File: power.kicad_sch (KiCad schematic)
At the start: 0 parts

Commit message: More work. Getting there.
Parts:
- added C18, C19, C20, C21, C22, C23, C24, C25, C26, C27, C28, C29, C30, C31: 0.1uF, symbol Device:C_Small
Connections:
- new net: C30.2, C31.2
- new net GND: C18.2, C19.2, C20.2, C21.2, C22.2, C23.2, C24.2, C25.2, C26.2, C27.2, C28.2, C29.2
- new net V5: C18.1, C19.1, C20.1, C21.1, C22.1, C23.1, C24.1, C25.1, C26.1, C27.1, C28.1, C29.1, C30.1, C31.1
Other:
- note added: "Bottom Side"
- note added: "Top Side"

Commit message: Latest updates
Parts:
- added C33: 47uF, symbol Device:C_Polarized_Small
- added D1: MBRS140, Diode_SMD:D_SOD-123F, symbol Device:D_Small
- added F1: ASMDC185F/33-2, symbol Device:Polyfuse_Small
- C18, C19, C20, C21, C22, C23, C24, C25, C26, C27, C28, C29, C30, C31: footprint (none) -> Capacitor_SMD:C_0603_1608Metric_Pad1.08x0.95mm_HandSolder
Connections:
- net GND: now also C33.2
- net V5: now also C33.1, D1.2 (A)
- new net: D1.1 (K), F1.1
- new net SCSI_TERMPWR: F1.2

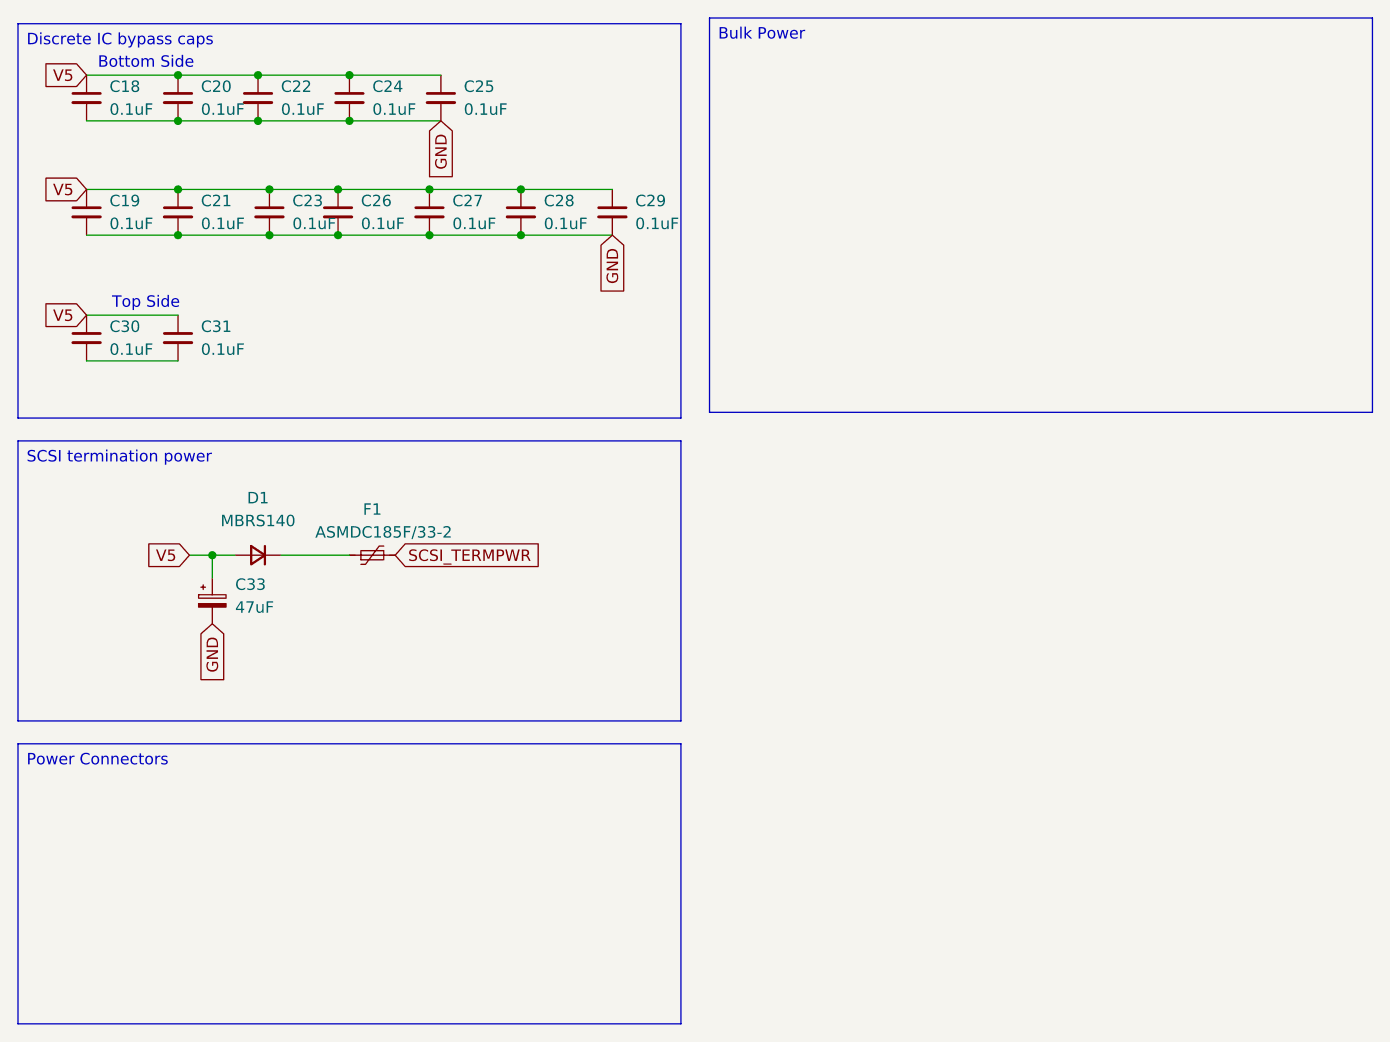
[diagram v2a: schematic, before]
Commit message: Finished first pass at new schematics
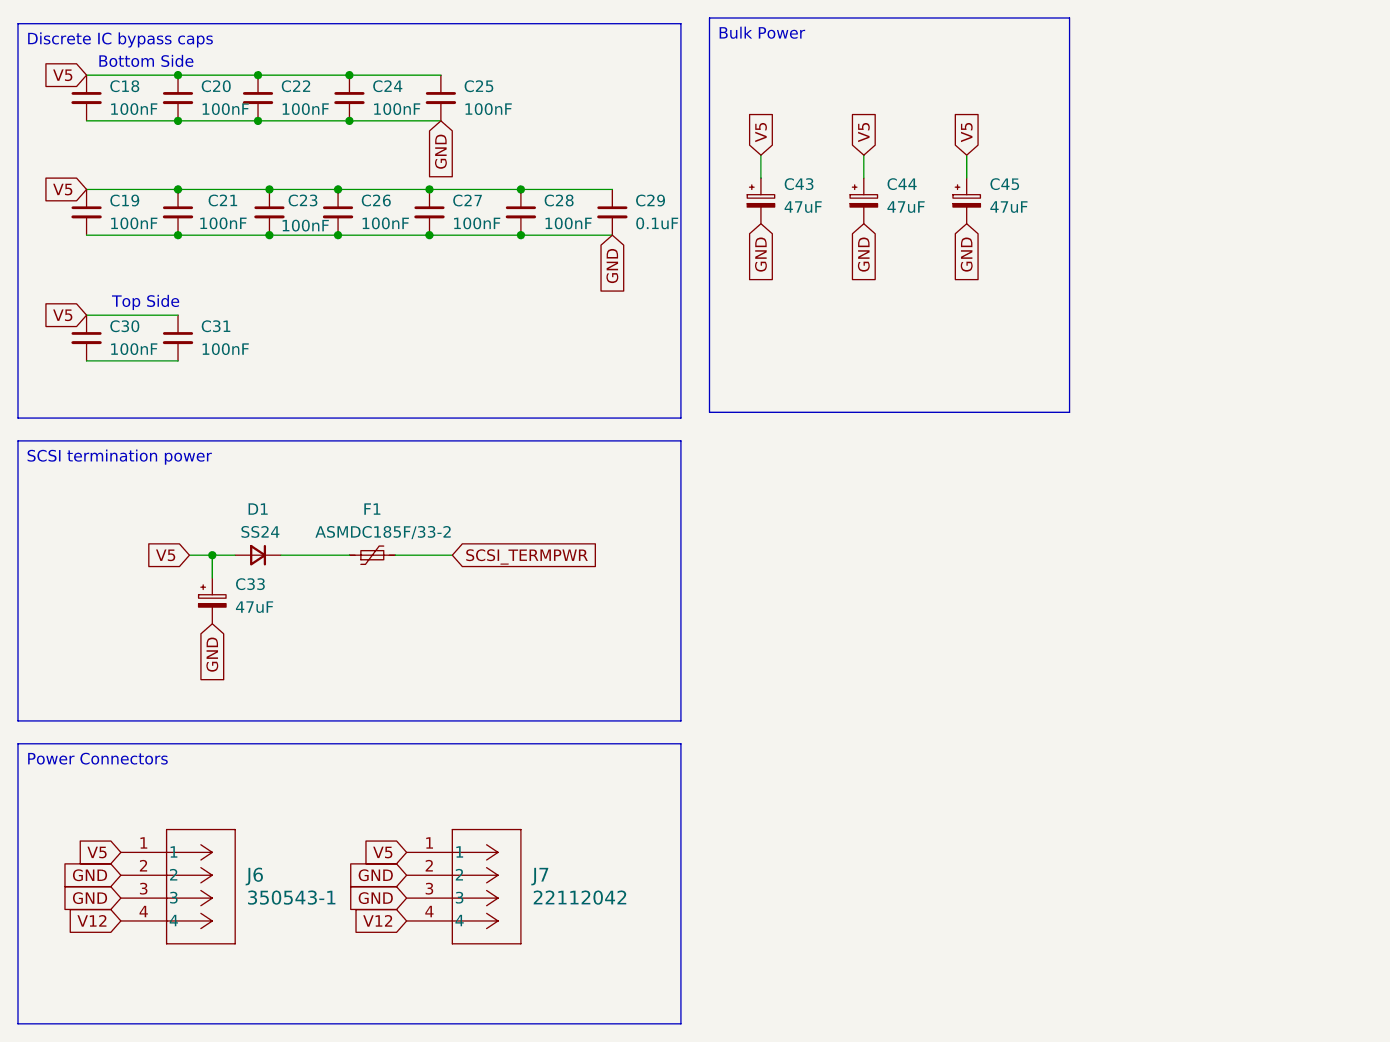
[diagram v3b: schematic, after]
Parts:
- added C43, C44, C45: 47uF, Capacitor_SMD:CP_Elec_6.3x7.7, symbol Device:C_Polarized_Small
- added J6: 350543-1, 350543_1:CONN_350543-1_TYC, symbol 350543_1:350543-1
- added J7: 22112042, 22112042:CONN_A-6373-04A_MOL, symbol 22112042:22112042
- C18, C19, C20, C21, C22, C23, C24, C25, C26, C27, C28, C30, C31: value 0.1uF -> 100nF
- C33: footprint (none) -> Capacitor_SMD:CP_Elec_6.3x7.7
- D1: value MBRS140 -> SS24; footprint Diode_SMD:D_SOD-123F -> Diode_SMD:D_SMA_Handsoldering
- F1: footprint (none) -> Fuse:Fuse_2920_7451Metric_Pad2.10x5.45mm_HandSolder
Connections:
- net GND: now also C43.2, C44.2, C45.2, J6.2, J6.3, J7.2, J7.3
- net V5: now also C43.1, C44.1, C45.1, J6.1, J7.1
- new net V12: J6.4, J7.4

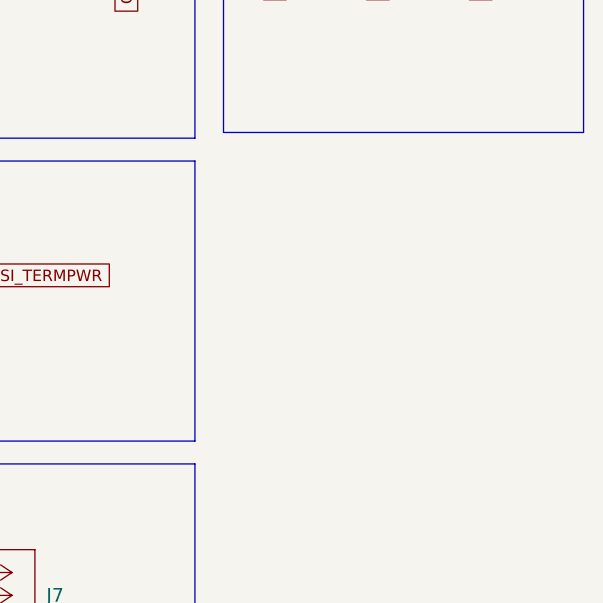
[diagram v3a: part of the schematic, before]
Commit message: Connect VCCINT on CPLD, add GND and V5 to power symbols
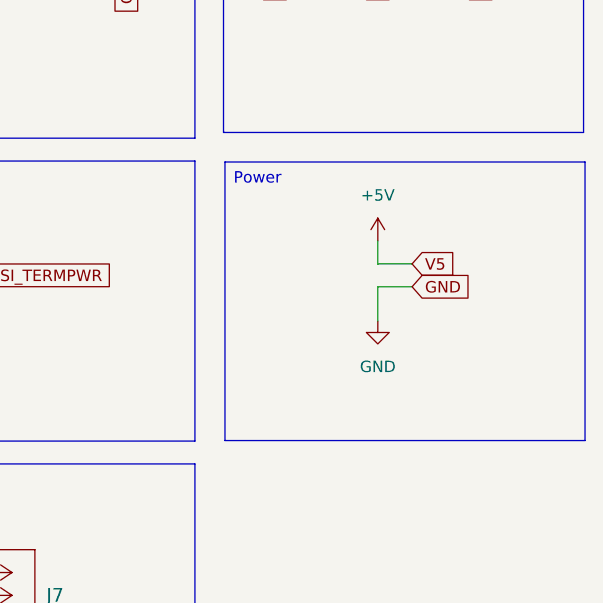
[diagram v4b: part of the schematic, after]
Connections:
- net V5 renamed +5V
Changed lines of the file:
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@@
+		)
+	)
+	(text_box "Power\n"
+		(exclude_from_sim no)
+		(at 98.5884 67.4165 0)
+		(size 40.005 30.9505)
+		(margins 0.9525 0.9525 0.9525 0.9525)
+		(stroke
+			(width 0)
+			(type solid)
+		)
+		(fill
+			(type none)
+		)
+		(effects
+			(font
+				(size 1.27 1.27)
+			)
+			(justify left top)
 		)
 	)
@@
 	(wire
 		(pts
+			(xy 115.57 81.28) (xy 119.38 81.28)
+		)
+		(stroke
+			(width 0)
+			(type default)
+		)
+	)
+	(wire
+		(pts
 			(xy 39.37 44.45) (xy 49.53 44.45)
 		)
@@
 	(wire
 		(pts
+			(xy 115.57 76.2) (xy 115.57 78.74)
+		)
+		(stroke
+			(width 0)
+			(type default)
+		)
+	)
+	(wire
+		(pts
 			(xy 67.31 44.45) (xy 77.47 44.45)
 		)
@@
 	(wire
 		(pts
+			(xy 115.57 85.09) (xy 115.57 81.28)
+		)
+		(stroke
+			(width 0)
+			(type default)
+		)
+	)
+	(wire
+		(pts
 			(xy 69.85 80.01) (xy 63.5 80.01)
 		)
@@
 	(wire
 		(pts
+			(xy 115.57 78.74) (xy 119.38 78.74)
+		)
+		(stroke
+			(width 0)
+			(type default)
+		)
+	)
+	(wire
+		(pts
 			(xy 58.42 26.67) (xy 68.58 26.67)
 		)
@@
 		)
 	)
+	(global_label "GND"
+		(shape input)
+		(at 119.38 81.28 0)
+		(fields_autoplaced yes)
+		(effects
+			(font
+				(size 1.27 1.27)
+			)
+			(justify left)
+		)
+		(property "Intersheetrefs" "${INTERSHEET_REFS}"
+			(at 126.2357 81.28 0)
+			(effects
+				(font
+					(size 1.27 1.27)
+				)
+				(justify left)
+				(hide yes)
+			)
+		)
+	)
 	(global_label "V5"
 		(shape input)
@@
 				)
 				(justify right)
+				(hide yes)
+			)
+		)
+	)
+	(global_label "V5"
+		(shape input)
+		(at 119.38 78.74 0)
+		(fields_autoplaced yes)
+		(effects
+			(font
+				(size 1.27 1.27)
+			)
+			(justify left)
+		)
+		(property "Intersheetrefs" "${INTERSHEET_REFS}"
+			(at 124.6633 78.74 0)
+			(effects
+				(font
+					(size 1.27 1.27)
+				)
+				(justify left)
 				(hide yes)
 			)
@@
 	)
 	(symbol
+		(lib_id "power:GND")
+		(at 115.57 85.09 0)
+		(unit 1)
+		(exclude_from_sim no)
+		(in_bom yes)
+		(on_board yes)
+		(dnp no)
+		(fields_autoplaced yes)
+		(property "Reference" "#PWR03"
+			(at 115.57 91.44 0)
+			(effects
+				(font
+					(size 1.27 1.27)
+				)
+				(hide yes)
+			)
+		)
+		(property "Value" "GND"
+			(at 115.57 90.17 0)
+			(effects
+				(font
+					(size 1.27 1.27)
+				)
+			)
+		)
+		(property "Footprint" ""
+			(at 115.57 85.09 0)
+			(effects
+				(font
+					(size 1.27 1.27)
+				)
+				(hide yes)
+			)
+		)
+		(property "Datasheet" ""
+			(at 115.57 85.09 0)
+			(effects
+				(font
+					(size 1.27 1.27)
+				)
+				(hide yes)
+			)
+		)
+		(property "Description" "Power symbol creates a global label with name \"GND\" , ground"
+			(at 115.57 85.09 0)
+			(effects
+				(font
+					(size 1.27 1.27)
+				)
+				(hide yes)
+			)
+		)
+		(pin "1"
+		)
+		(instances
+			(project ""
+				(path "/8f9f4021-47aa-41d9-bea7-f6ccf72098bb/166c366c-e5f9-4398-87d9-75fc4b57be99"
+					(reference "#PWR03")
+					(unit 1)
+				)
+			)
+		)
+	)
+	(symbol
 		(lib_id "Device:C_Small")
 		(at 87.63 41.91 0)
@@
 					(unit 1)
 				)
+			)
+		)
+	)
+	(symbol
+		(lib_id "power:+5V")
+		(at 115.57 76.2 0)
+		(unit 1)
+		(exclude_from_sim no)
+		(in_bom yes)
+		(on_board yes)
+		(dnp no)
+		(fields_autoplaced yes)
+		(property "Reference" "#PWR02"
+			(at 115.57 80.01 0)
+			(effects
+				(font
+					(size 1.27 1.27)
+				)
+				(hide yes)
+			)
+		)
+		(property "Value" "+5V"
+			(at 115.57 71.12 0)
+			(effects
+				(font
+					(size 1.27 1.27)
+				)
+			)
+		)
+		(property "Footprint" ""
+			(at 115.57 76.2 0)
+			(effects
+				(font
+					(size 1.27 1.27)
+				)
+				(hide yes)
+			)
+		)
+		(property "Datasheet" ""
+			(at 115.57 76.2 0)
+			(effects
+				(font
+					(size 1.27 1.27)
+				)
+				(hide yes)
+			)
+		)
+		(property "Description" "Power symbol creates a global label with name \"+5V\""
+			(at 115.57 76.2 0)
+			(effects
+				(font
+					(size 1.27 1.27)
+				)
+				(hide yes)
+			)
+		)
+		(pin "1"
+		)
+		(instances
+			(project ""
+				(path "/8f9f4021-47aa-41d9-bea7-f6ccf72098bb/166c366c-e5f9-4398-87d9-75fc4b57be99"
+					(reference "#PWR02")
+					(unit 1)
+				)
